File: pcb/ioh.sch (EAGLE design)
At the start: 32 parts, among them Q1 MOSFET-NCHANNEL2N7000, Q2 MOSFET-NCHANNEL2N7000, Q3 MOSFET-NCHANNEL2N7000, Q4 MOSFET-NCHANNEL2N7000

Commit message: ftdi connector
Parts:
- added D1: (no value), SparkFun-DiscreteSemi:DIODEKIT
- added JP3: FTDI_DEVICE, SparkFun-Connectors:FTDI_DEVICE
- renumbered Q1 to QBLINK, Q2 to QFRONT, Q3 to QBACK, Q4 to QVIBE
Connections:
- removed net N$14: JP2.1, U$1.TX0
- new net SPIMISO: JP1.4, JP3.CTS, U$1.SPIMISO
- new net TX0: JP2.1, JP3.RXI, U$1.TX0
- net GND: now also JP3.GND
- net N$7: now also D1.A, JP3.TXO; no longer JP1.4, U$1.SPIMISO
- net RXBACK: now also D1.C
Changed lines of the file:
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@@
 <part name="LED5" library="adafruit" deviceset="WS2812" device=""/>
 <part name="GND3" library="SparkFun-Aesthetics" deviceset="GND" device=""/>
-<part name="Q1" library="SparkFun-DiscreteSemi" deviceset="MOSFET-NCHANNEL" device="2N7000"/>
+<part name="QBLINK" library="SparkFun-DiscreteSemi" deviceset="MOSFET-NCHANNEL" device="2N7000"/>
 <part name="GND4" library="SparkFun-Aesthetics" deviceset="GND" device=""/>
 <part name="SUPPLY5" library="SparkFun-Aesthetics" deviceset="VCC" device=""/>
@@
 <part name="SUPPLY6" library="SparkFun-Aesthetics" deviceset="VCC" device=""/>
 <part name="R2" library="SparkFun-Resistors" deviceset="RESISTOR" device="PTH-1/4W" value="20k"/>
-<part name="Q2" library="SparkFun-DiscreteSemi" deviceset="MOSFET-NCHANNEL" device="2N7000"/>
+<part name="QFRONT" library="SparkFun-DiscreteSemi" deviceset="MOSFET-NCHANNEL" device="2N7000"/>
 <part name="GND5" library="SparkFun-Aesthetics" deviceset="GND" device=""/>
 <part name="IRBACK" library="SparkFun-LED" deviceset="LTE-302" device=""/>
 <part name="SUPPLY7" library="SparkFun-Aesthetics" deviceset="VCC" device=""/>
 <part name="R3" library="SparkFun-Resistors" deviceset="RESISTOR" device="PTH-1/4W" value="20k"/>
-<part name="Q3" library="SparkFun-DiscreteSemi" deviceset="MOSFET-NCHANNEL" device="2N7000"/>
+<part name="QBACK" library="SparkFun-DiscreteSemi" deviceset="MOSFET-NCHANNEL" device="2N7000"/>
 <part name="GND6" library="SparkFun-Aesthetics" deviceset="GND" device=""/>
 <part name="RXFRONT" library="ioh-1" deviceset="TSOP2438" device=""/>
@@
 <part name="SUPPLY10" library="SparkFun-Aesthetics" deviceset="VCC" device=""/>
 <part name="GND9" library="SparkFun-Aesthetics" deviceset="GND" device=""/>
-<part name="Q4" library="SparkFun-DiscreteSemi" deviceset="MOSFET-NCHANNEL" device="2N7000"/>
+<part name="QVIBE" library="SparkFun-DiscreteSemi" deviceset="MOSFET-NCHANNEL" device="2N7000"/>
 <part name="S1" library="adafruit" deviceset="40-XX" device=""/>
 <part name="GND10" library="SparkFun-Aesthetics" deviceset="GND" device=""/>
@@
 <part name="TX-BACK" library="SparkFun-Passives" deviceset="JUMPER-PAD-2-NC_BY_TRACE" device=""/>
 <part name="TX-FRONT" library="SparkFun-Passives" deviceset="JUMPER-PAD-2-NC_BY_TRACE" device=""/>
+<part name="JP3" library="SparkFun-Connectors" deviceset="FTDI_DEVICE" device=""/>
+<part name="GND11" library="SparkFun-Aesthetics" deviceset="GND" device=""/>
+<part name="D1" library="SparkFun-DiscreteSemi" deviceset="DIODE" device="KIT"/>
 </parts>
 <sheets>
@@
 <instance part="LED5" gate="G$1" x="104.14" y="119.38"/>
 <instance part="GND3" gate="1" x="58.42" y="101.6"/>
-<instance part="Q1" gate="G$1" x="-38.1" y="81.28"/>
+<instance part="QBLINK" gate="G$1" x="-38.1" y="81.28"/>
 <instance part="GND4" gate="1" x="-38.1" y="68.58"/>
 <instance part="SUPPLY5" gate="G$1" x="-38.1" y="106.68"/>
@@
 <instance part="SUPPLY6" gate="G$1" x="-96.52" y="193.04"/>
 <instance part="R2" gate="G$1" x="-96.52" y="185.42" rot="R90"/>
-<instance part="Q2" gate="G$1" x="-96.52" y="157.48"/>
+<instance part="QFRONT" gate="G$1" x="-96.52" y="157.48"/>
 <instance part="GND5" gate="1" x="-96.52" y="144.78"/>
 <instance part="IRBACK" gate="G$1" x="-30.48" y="172.72"/>
 <instance part="SUPPLY7" gate="G$1" x="-30.48" y="193.04"/>
 <instance part="R3" gate="G$1" x="-30.48" y="185.42" rot="R90"/>
-<instance part="Q3" gate="G$1" x="-30.48" y="157.48"/>
+<instance part="QBACK" gate="G$1" x="-30.48" y="157.48"/>
 <instance part="GND6" gate="1" x="-30.48" y="144.78"/>
 <instance part="RXFRONT" gate="G$1" x="-129.54" y="116.84" rot="R270"/>
@@
 <instance part="SUPPLY10" gate="G$1" x="15.24" y="190.5"/>
 <instance part="GND9" gate="1" x="15.24" y="152.4"/>
-<instance part="Q4" gate="G$1" x="15.24" y="162.56"/>
+<instance part="QVIBE" gate="G$1" x="15.24" y="162.56"/>
 <instance part="S1" gate="1" x="-114.3" y="63.5"/>
 <instance part="GND10" gate="1" x="-114.3" y="45.72"/>
@@
 <instance part="TX-BACK" gate="G$1" x="-48.26" y="157.48"/>
 <instance part="TX-FRONT" gate="G$1" x="-114.3" y="157.48"/>
+<instance part="JP3" gate="G$1" x="109.22" y="177.8"/>
+<instance part="GND11" gate="1" x="99.06" y="162.56"/>
+<instance part="D1" gate="G$1" x="99.06" y="180.34" rot="R180"/>
 </instances>
 <busses>
@@
 </segment>
 </net>
-<net name="N$7" class="0">
+<net name="SPIMISO" class="0">
 <segment>
 <pinref part="JP1" gate="G$1" pin="4"/>
@@
 <wire x1="17.78" y1="76.2" x2="27.94" y2="76.2" width="0.1524" layer="91"/>
 </segment>
+<segment>
+<pinref part="JP3" gate="G$1" pin="CTS"/>
+<wire x1="104.14" y1="172.72" x2="88.9" y2="172.72" width="0.1524" layer="91"/>
+<label x="88.9" y="172.72" size="1.778" layer="95"/>
+</segment>
 </net>
 <net name="N$8" class="0">
@@
 </segment>
 </net>
-<net name="N$14" class="0">
+<net name="TX0" class="0">
 <segment>
 <pinref part="U$1" gate="G$1" pin="TX0"/>
 <pinref part="JP2" gate="G$1" pin="1"/>
 <wire x1="68.58" y1="60.96" x2="81.28" y2="60.96" width="0.1524" layer="91"/>
+</segment>
+<segment>
+<pinref part="JP3" gate="G$1" pin="RXI"/>
+<wire x1="104.14" y1="177.8" x2="88.9" y2="177.8" width="0.1524" layer="91"/>
+<label x="88.9" y="177.8" size="1.778" layer="95"/>
 </segment>
 </net>
@@
 </segment>
 <segment>
-<pinref part="Q1" gate="G$1" pin="S"/>
+<pinref part="QBLINK" gate="G$1" pin="S"/>
 <pinref part="GND4" gate="1" pin="GND"/>
 <wire x1="-38.1" y1="76.2" x2="-38.1" y2="71.12" width="0.1524" layer="91"/>
 </segment>
 <segment>
-<pinref part="Q2" gate="G$1" pin="S"/>
+<pinref part="QFRONT" gate="G$1" pin="S"/>
 <pinref part="GND5" gate="1" pin="GND"/>
 <wire x1="-96.52" y1="152.4" x2="-96.52" y2="147.32" width="0.1524" layer="91"/>
 </segment>
 <segment>
-<pinref part="Q3" gate="G$1" pin="S"/>
+<pinref part="QBACK" gate="G$1" pin="S"/>
 <pinref part="GND6" gate="1" pin="GND"/>
 <wire x1="-30.48" y1="152.4" x2="-30.48" y2="147.32" width="0.1524" layer="91"/>
@@
 <segment>
 <pinref part="GND9" gate="1" pin="GND"/>
-<pinref part="Q4" gate="G$1" pin="S"/>
+<pinref part="QVIBE" gate="G$1" pin="S"/>
 <wire x1="15.24" y1="154.94" x2="15.24" y2="157.48" width="0.1524" layer="91"/>
 </segment>
@@
 <wire x1="-111.76" y1="55.88" x2="-114.3" y2="55.88" width="0.1524" layer="91"/>
 <junction x="-114.3" y="55.88"/>
+</segment>
+<segment>
+<pinref part="JP3" gate="G$1" pin="GND"/>
+<pinref part="GND11" gate="1" pin="GND"/>
+<wire x1="104.14" y1="170.18" x2="99.06" y2="170.18" width="0.1524" layer="91"/>
+<wire x1="99.06" y1="170.18" x2="99.06" y2="165.1" width="0.1524" layer="91"/>
 </segment>
 </net>
@@
 <segment>
 <pinref part="R1" gate="G$1" pin="1"/>
-<pinref part="Q1" gate="G$1" pin="D"/>
+<pinref part="QBLINK" gate="G$1" pin="D"/>
 <wire x1="-38.1" y1="93.98" x2="-38.1" y2="91.44" width="0.1524" layer="91"/>
 <wire x1="-38.1" y1="91.44" x2="-38.1" y2="86.36" width="0.1524" layer="91"/>
@@
 <segment>
 <pinref part="IRFRONT" gate="G$1" pin="C"/>
-<pinref part="Q2" gate="G$1" pin="D"/>
+<pinref part="QFRONT" gate="G$1" pin="D"/>
 <wire x1="-96.52" y1="167.64" x2="-96.52" y2="162.56" width="0.1524" layer="91"/>
 </segment>
@@
 <segment>
 <pinref part="IRBACK" gate="G$1" pin="C"/>
-<pinref part="Q3" gate="G$1" pin="D"/>
+<pinref part="QBACK" gate="G$1" pin="D"/>
 <wire x1="-30.48" y1="167.64" x2="-30.48" y2="162.56" width="0.1524" layer="91"/>
 </segment>
@@
 <label x="-60.96" y="99.06" size="1.778" layer="95"/>
 </segment>
+<segment>
+<pinref part="D1" gate="G$1" pin="C"/>
+<wire x1="96.52" y1="180.34" x2="88.9" y2="180.34" width="0.1524" layer="91"/>
+<label x="88.9" y="180.34" size="1.778" layer="95"/>
+</segment>
 </net>
 <net name="N$13" class="0">
 <segment>
-<pinref part="Q4" gate="G$1" pin="D"/>
+<pinref part="QVIBE" gate="G$1" pin="D"/>
 <pinref part="BZZ" gate="G$1" pin="2"/>
 <wire x1="15.24" y1="167.64" x2="15.24" y2="172.72" width="0.1524" layer="91"/>
@@
 <net name="VIBE" class="0">
 <segment>
-<pinref part="Q4" gate="G$1" pin="G"/>
+<pinref part="QVIBE" gate="G$1" pin="G"/>
 <wire x1="7.62" y1="162.56" x2="-10.16" y2="162.56" width="0.1524" layer="91"/>
 <label x="-10.16" y="162.56" size="1.778" layer="95"/>
@@
 <net name="N$6" class="0">
 <segment>
-<pinref part="Q1" gate="G$1" pin="G"/>
+<pinref part="QBLINK" gate="G$1" pin="G"/>
 <pinref part="BLINK" gate="G$1" pin="2"/>
 <wire x1="-45.72" y1="81.28" x2="-48.26" y2="81.28" width="0.1524" layer="91"/>
@@
 <segment>
 <pinref part="TX-FRONT" gate="G$1" pin="2"/>
-<pinref part="Q2" gate="G$1" pin="G"/>
+<pinref part="QFRONT" gate="G$1" pin="G"/>
 <wire x1="-109.22" y1="157.48" x2="-104.14" y2="157.48" width="0.1524" layer="91"/>
 </segment>
@@
 <segment>
 <pinref part="TX-BACK" gate="G$1" pin="2"/>
-<pinref part="Q3" gate="G$1" pin="G"/>
+<pinref part="QBACK" gate="G$1" pin="G"/>
 <wire x1="-43.18" y1="157.48" x2="-38.1" y2="157.48" width="0.1524" layer="91"/>
 </segment>
 </net>
+<net name="N$7" class="0">
+<segment>
+<pinref part="JP3" gate="G$1" pin="TXO"/>
+<pinref part="D1" gate="G$1" pin="A"/>
+<wire x1="104.14" y1="180.34" x2="101.6" y2="180.34" width="0.1524" layer="91"/>
+</segment>
+</net>

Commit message: add labels; connect boop
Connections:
- removed net N$19: JP2.6, U$1.RTS0
- net BOOP: now also JP2.6, U$1.RTS0
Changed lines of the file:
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@@
 <pinref part="U$1" gate="G$1" pin="SPIMISO"/>
 <wire x1="17.78" y1="76.2" x2="27.94" y2="76.2" width="0.1524" layer="91"/>
+<label x="17.78" y="76.2" size="1.778" layer="95"/>
 </segment>
 <segment>
@@
 <pinref part="JP2" gate="G$1" pin="1"/>
 <wire x1="68.58" y1="60.96" x2="81.28" y2="60.96" width="0.1524" layer="91"/>
+<label x="68.58" y="60.96" size="1.778" layer="95"/>
 </segment>
 <segment>
@@
 <pinref part="JP2" gate="G$1" pin="5"/>
 <wire x1="68.58" y1="71.12" x2="81.28" y2="71.12" width="0.1524" layer="91"/>
-</segment>
-</net>
-<net name="N$19" class="0">
-<segment>
-<pinref part="U$1" gate="G$1" pin="RTS0"/>
-<pinref part="JP2" gate="G$1" pin="6"/>
-<wire x1="68.58" y1="73.66" x2="81.28" y2="73.66" width="0.1524" layer="91"/>
 </segment>
 </net>
@@
 <label x="-96.52" y="71.12" size="1.778" layer="95"/>
 </segment>
-</net>
+<segment>
+<pinref part="U$1" gate="G$1" pin="RTS0"/>
+<pinref part="JP2" gate="G$1" pin="6"/>
+<wire x1="68.58" y1="73.66" x2="81.28" y2="73.66" width="0.1524" layer="91"/>
+<label x="68.58" y="73.66" size="1.778" layer="95"/>
+</segment>
+</net>

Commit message: moved stuff around; put it in a box
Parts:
- added FRAME1: FRAME-LEDGER, SparkFun-Aesthetics:FRAME-LEDGER
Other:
- note removed: "TODO FTDI"
- moved on the sheet: BAT1, BAT2, C1, D1, GND, JP3, S1, VCC, VCCIO

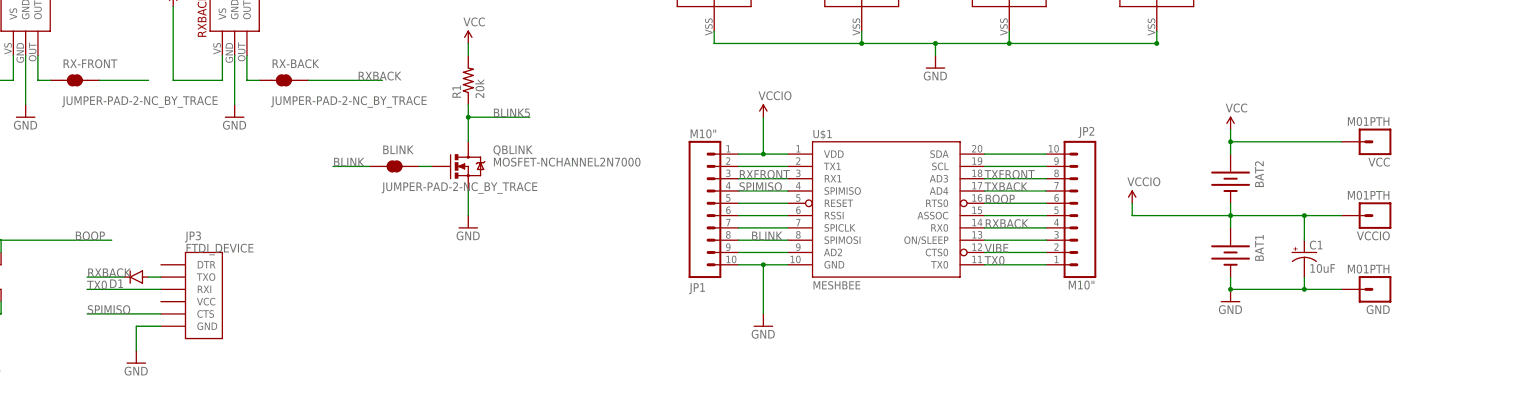
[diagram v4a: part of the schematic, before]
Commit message: place bsides logo
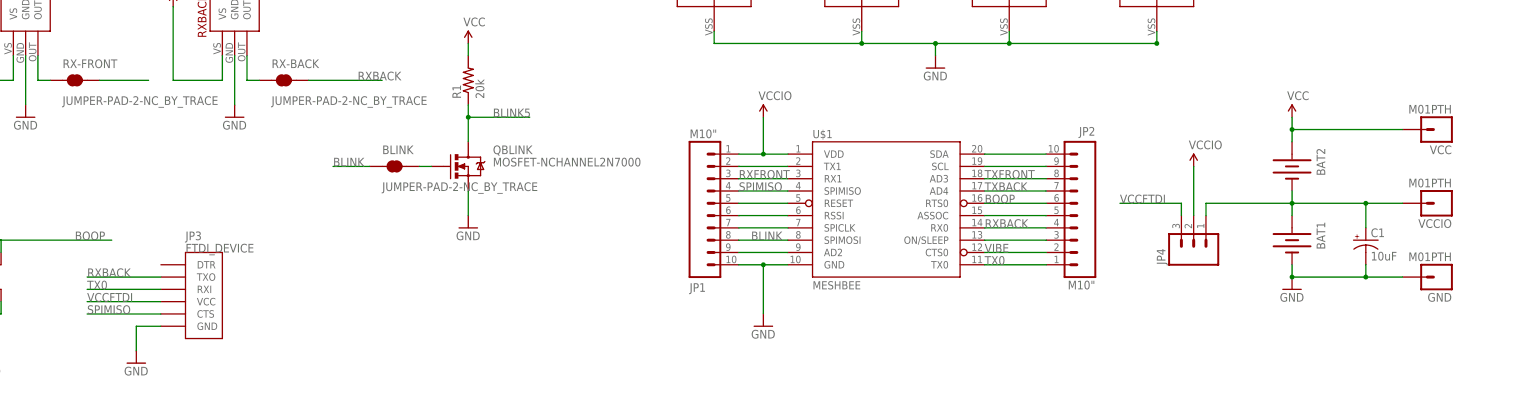
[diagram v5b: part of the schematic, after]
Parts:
- removed D1: (no value), SparkFun-DiscreteSemi:DIODEKIT
- added JP4: (no value), SparkFun-Connectors:M03LOCK
- added U$2: BSIDES, ioh-1:BSIDES
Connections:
- removed net N$7: D1.A, JP3.TXO
- new net N$14: BAT1.+, BAT2.-, C1.+, JP4.1, VCCIO.1
- new net VCCFTDI: JP3.VCC, JP4.3
- net RXBACK: now also JP3.TXO; no longer D1.C
- net VCCIO: no longer BAT1.+, BAT2.-, C1.+, VCCIO.1
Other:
- moved on the sheet: BAT1, BAT2, C1, GND, VCC, VCCIO
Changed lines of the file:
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@@
 <layer number="223" name="223bmp" color="24" fill="1" visible="no" active="no"/>
 <layer number="224" name="224bmp" color="25" fill="1" visible="no" active="no"/>
+<layer number="225" name="225bmp" color="26" fill="10" visible="yes" active="yes"/>
+<layer number="226" name="226bmp" color="27" fill="10" visible="yes" active="yes"/>
+<layer number="227" name="227bmp" color="28" fill="10" visible="yes" active="yes"/>
+<layer number="228" name="228bmp" color="29" fill="10" visible="yes" active="yes"/>
+<layer number="229" name="229bmp" color="30" fill="10" visible="yes" active="yes"/>
+<layer number="230" name="230bmp" color="31" fill="10" visible="yes" active="yes"/>
+<layer number="231" name="231bmp" color="32" fill="10" visible="yes" active="yes"/>
 <layer number="248" name="Housing" color="7" fill="1" visible="yes" active="yes"/>
 <layer number="249" name="Edge" color="7" fill="1" visible="yes" active="yes"/>
@@
 <part name="JP3" library="SparkFun-Connectors" deviceset="FTDI_DEVICE" device=""/>
 <part name="GND11" library="SparkFun-Aesthetics" deviceset="GND" device=""/>
-<part name="D1" library="SparkFun-DiscreteSemi" deviceset="DIODE" device="KIT"/>
 <part name="FRAME1" library="SparkFun-Aesthetics" deviceset="FRAME-LEDGER" device=""/>
+<part name="JP4" library="SparkFun-Connectors" deviceset="M03" device="LOCK"/>
+<part name="U$2" library="ioh-1" deviceset="BSIDES" device=""/>
 </parts>
 <sheets>
@@
 <instances>
 <instance part="U$1" gate="G$1" x="48.26" y="71.12"/>
-<instance part="BAT1" gate="G$1" x="119.38" y="63.5" rot="R270"/>
-<instance part="BAT2" gate="G$1" x="119.38" y="78.74" rot="R270"/>
+<instance part="BAT1" gate="G$1" x="132.08" y="66.04" rot="R270"/>
+<instance part="BAT2" gate="G$1" x="132.08" y="81.28" rot="R270"/>
 <instance part="JP1" gate="G$1" x="7.62" y="66.04" rot="MR180"/>
 <instance part="JP2" gate="G$1" x="91.44" y="78.74" rot="MR0"/>
-<instance part="GND1" gate="1" x="119.38" y="53.34"/>
-<instance part="SUPPLY1" gate="G$1" x="99.06" y="73.66"/>
-<instance part="SUPPLY2" gate="G$1" x="119.38" y="88.9"/>
+<instance part="GND1" gate="1" x="132.08" y="55.88"/>
+<instance part="SUPPLY1" gate="G$1" x="111.76" y="81.28"/>
+<instance part="SUPPLY2" gate="G$1" x="132.08" y="91.44"/>
 <instance part="GND2" gate="1" x="22.86" y="48.26"/>
 <instance part="SUPPLY3" gate="G$1" x="22.86" y="91.44"/>
@@
 <instance part="GND8" gate="1" x="-86.36" y="91.44"/>
 <instance part="SUPPLY9" gate="G$1" x="-99.06" y="114.3"/>
-<instance part="C1" gate="G$1" x="134.62" y="63.5"/>
+<instance part="C1" gate="G$1" x="147.32" y="66.04"/>
 <instance part="BZZ" gate="G$1" x="30.48" y="175.26" rot="R180"/>
 <instance part="SUPPLY10" gate="G$1" x="15.24" y="190.5"/>
@@
 <instance part="S1" gate="1" x="-137.16" y="58.42"/>
 <instance part="GND10" gate="1" x="-137.16" y="40.64"/>
-<instance part="VCC" gate="G$1" x="149.86" y="86.36" rot="R180"/>
-<instance part="VCCIO" gate="G$1" x="149.86" y="71.12" rot="R180"/>
-<instance part="GND" gate="G$1" x="149.86" y="55.88" rot="R180"/>
+<instance part="VCC" gate="G$1" x="162.56" y="88.9" rot="R180"/>
+<instance part="VCCIO" gate="G$1" x="162.56" y="73.66" rot="R180"/>
+<instance part="GND" gate="G$1" x="162.56" y="58.42" rot="R180"/>
 <instance part="LOGO1" gate="G$1" x="96.52" y="-33.02"/>
 <instance part="BLINK" gate="G$1" x="-53.34" y="81.28"/>
@@
 <instance part="JP3" gate="G$1" x="-96.52" y="55.88"/>
 <instance part="GND11" gate="1" x="-106.68" y="40.64"/>
-<instance part="D1" gate="G$1" x="-106.68" y="58.42" rot="R180"/>
 <instance part="FRAME1" gate="G$1" x="-210.82" y="-50.8"/>
 <instance part="FRAME1" gate="G$2" x="119.38" y="-50.8"/>
+<instance part="JP4" gate="G$1" x="111.76" y="63.5" rot="R90"/>
+<instance part="U$2" gate="G$1" x="99.06" y="-20.32" rot="MR0"/>
 </instances>
 <busses>
@@
 <pinref part="BAT1" gate="G$1" pin="-"/>
 <pinref part="GND1" gate="1" pin="GND"/>
-<wire x1="119.38" y1="58.42" x2="119.38" y2="55.88" width="0.1524" layer="91"/>
+<wire x1="132.08" y1="60.96" x2="132.08" y2="58.42" width="0.1524" layer="91"/>
 <pinref part="C1" gate="G$1" pin="-"/>
-<wire x1="134.62" y1="58.42" x2="134.62" y2="55.88" width="0.1524" layer="91"/>
-<wire x1="134.62" y1="55.88" x2="119.38" y2="55.88" width="0.1524" layer="91"/>
-<junction x="119.38" y="55.88"/>
+<wire x1="147.32" y1="60.96" x2="147.32" y2="58.42" width="0.1524" layer="91"/>
+<wire x1="147.32" y1="58.42" x2="132.08" y2="58.42" width="0.1524" layer="91"/>
+<junction x="132.08" y="58.42"/>
 <pinref part="GND" gate="G$1" pin="1"/>
-<wire x1="142.24" y1="55.88" x2="134.62" y2="55.88" width="0.1524" layer="91"/>
-<junction x="134.62" y="55.88"/>
+<wire x1="154.94" y1="58.42" x2="147.32" y2="58.42" width="0.1524" layer="91"/>
+<junction x="147.32" y="58.42"/>
 </segment>
 <segment>
@@
 <segment>
 <pinref part="SUPPLY1" gate="G$1" pin="VCCIO"/>
-<wire x1="99.06" y1="73.66" x2="99.06" y2="71.12" width="0.1524" layer="91"/>
-<pinref part="BAT2" gate="G$1" pin="-"/>
-<pinref part="BAT1" gate="G$1" pin="+"/>
-<wire x1="119.38" y1="73.66" x2="119.38" y2="71.12" width="0.1524" layer="91"/>
-<wire x1="119.38" y1="71.12" x2="119.38" y2="68.58" width="0.1524" layer="91"/>
-<wire x1="99.06" y1="71.12" x2="119.38" y2="71.12" width="0.1524" layer="91"/>
-<junction x="119.38" y="71.12"/>
-<pinref part="C1" gate="G$1" pin="+"/>
-<wire x1="134.62" y1="66.04" x2="134.62" y2="71.12" width="0.1524" layer="91"/>
-<wire x1="134.62" y1="71.12" x2="119.38" y2="71.12" width="0.1524" layer="91"/>
-<pinref part="VCCIO" gate="G$1" pin="1"/>
-<wire x1="142.24" y1="71.12" x2="134.62" y2="71.12" width="0.1524" layer="91"/>
-<junction x="134.62" y="71.12"/>
+<wire x1="111.76" y1="81.28" x2="111.76" y2="71.12" width="0.1524" layer="91"/>
 </segment>
 <segment>
@@
 <pinref part="SUPPLY2" gate="G$1" pin="VCC"/>
 <pinref part="BAT2" gate="G$1" pin="+"/>
-<wire x1="119.38" y1="88.9" x2="119.38" y2="86.36" width="0.1524" layer="91"/>
+<wire x1="132.08" y1="91.44" x2="132.08" y2="88.9" width="0.1524" layer="91"/>
 <pinref part="VCC" gate="G$1" pin="1"/>
-<wire x1="119.38" y1="86.36" x2="119.38" y2="83.82" width="0.1524" layer="91"/>
-<wire x1="142.24" y1="86.36" x2="119.38" y2="86.36" width="0.1524" layer="91"/>
-<junction x="119.38" y="86.36"/>
+<wire x1="132.08" y1="88.9" x2="132.08" y2="86.36" width="0.1524" layer="91"/>
+<wire x1="154.94" y1="88.9" x2="132.08" y2="88.9" width="0.1524" layer="91"/>
+<junction x="132.08" y="88.9"/>
 </segment>
 <segment>
@@
 </segment>
 <segment>
-<pinref part="D1" gate="G$1" pin="C"/>
-<wire x1="-109.22" y1="58.42" x2="-116.84" y2="58.42" width="0.1524" layer="91"/>
 <label x="-116.84" y="58.42" size="1.778" layer="95"/>
+<pinref part="JP3" gate="G$1" pin="TXO"/>
+<wire x1="-101.6" y1="58.42" x2="-116.84" y2="58.42" width="0.1524" layer="91"/>
 </segment>
 </net>
@@
 </segment>
 </net>
-<net name="N$7" class="0">
-<segment>
-<pinref part="JP3" gate="G$1" pin="TXO"/>
-<pinref part="D1" gate="G$1" pin="A"/>
-<wire x1="-101.6" y1="58.42" x2="-104.14" y2="58.42" width="0.1524" layer="91"/>
-</segment>
-</net>
+<net name="N$14" class="0">
+<segment>
+<pinref part="BAT2" gate="G$1" pin="-"/>
+<pinref part="BAT1" gate="G$1" pin="+"/>
+<wire x1="132.08" y1="76.2" x2="132.08" y2="73.66" width="0.1524" layer="91"/>
+<wire x1="132.08" y1="73.66" x2="132.08" y2="71.12" width="0.1524" layer="91"/>
+<junction x="132.08" y="73.66"/>
+<pinref part="C1" gate="G$1" pin="+"/>
+<wire x1="147.32" y1="68.58" x2="147.32" y2="73.66" width="0.1524" layer="91"/>
+<wire x1="147.32" y1="73.66" x2="132.08" y2="73.66" width="0.1524" layer="91"/>
+<pinref part="VCCIO" gate="G$1" pin="1"/>
+<wire x1="154.94" y1="73.66" x2="147.32" y2="73.66" width="0.1524" layer="91"/>
+<junction x="147.32" y="73.66"/>
+<wire x1="132.08" y1="73.66" x2="114.3" y2="73.66" width="0.1524" layer="91"/>
+<pinref part="JP4" gate="G$1" pin="1"/>
+<wire x1="114.3" y1="73.66" x2="114.3" y2="71.12" width="0.1524" layer="91"/>
+</segment>
+</net>
+<net name="VCCFTDI" class="0">
+<segment>
+<pinref part="JP3" gate="G$1" pin="VCC"/>
+<wire x1="-101.6" y1="53.34" x2="-116.84" y2="53.34" width="0.1524" layer="91"/>
+<label x="-116.84" y="53.34" size="1.778" layer="95"/>
+</segment>
+<segment>
+<pinref part="JP4" gate="G$1" pin="3"/>
+<wire x1="109.22" y1="71.12" x2="109.22" y2="73.66" width="0.1524" layer="91"/>
+<wire x1="109.22" y1="73.66" x2="96.52" y2="73.66" width="0.1524" layer="91"/>
+<label x="96.52" y="73.66" size="1.778" layer="95"/>
+</segment>
+</net>

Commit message: move to origin
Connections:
- net VCCIO: now also JP4.2
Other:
- moved on the sheet: BAT1, BAT2, BLINK, BZZ, C1, GND, IRBACK, IRFRONT, JP1, JP2, JP3, JP4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
